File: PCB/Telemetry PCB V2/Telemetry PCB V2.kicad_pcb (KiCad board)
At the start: 4 copper layers, 70 x 70 mm, 51 parts, among them IC1 E22-900M22S, J1 USB_C_Receptacle_USB2.0_16P, J2 DBG/PGRM Hdr., J3 DATA IN, J4 GPS, J5 Battery, SW1 SW_MEC_5E, SW2 SW_MEC_5E, U1 STM32F411CEUx, U2 MCP1700x-250xxTT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

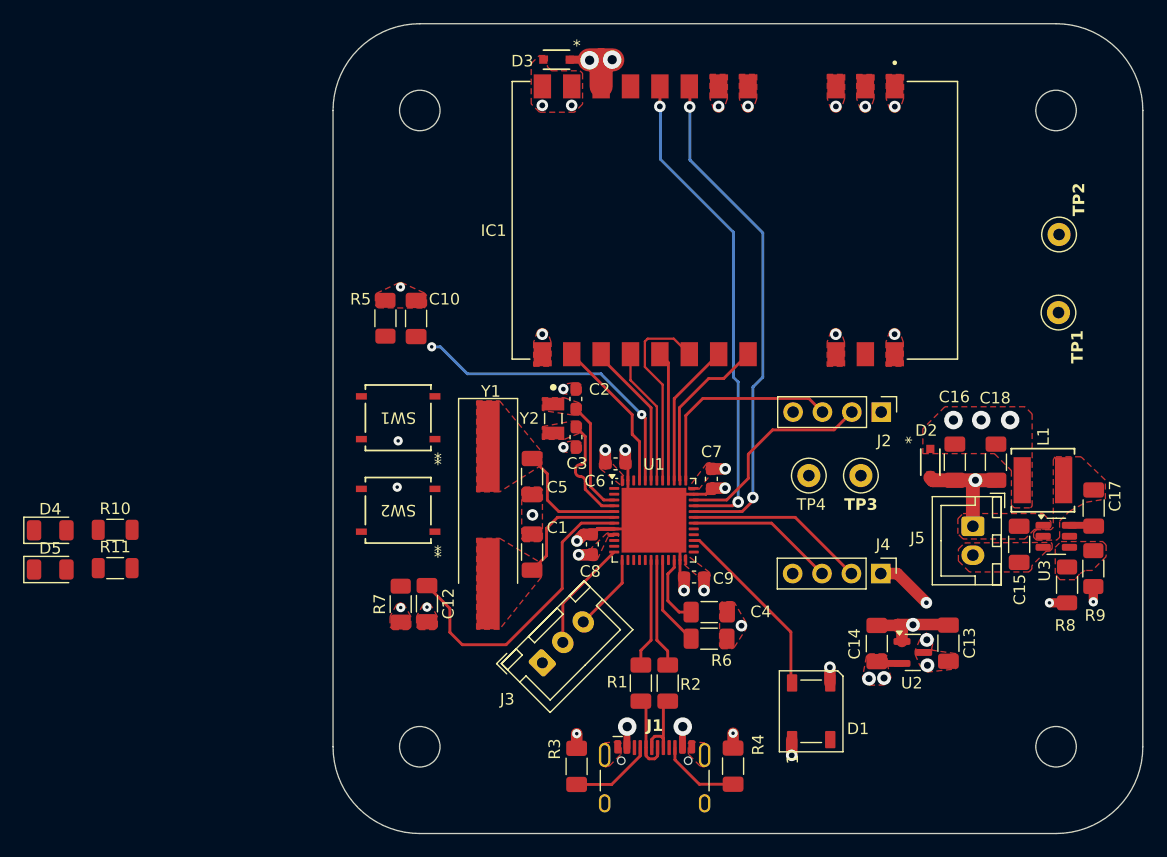
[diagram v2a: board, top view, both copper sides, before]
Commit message: Finished updating board to reflect issues and new components
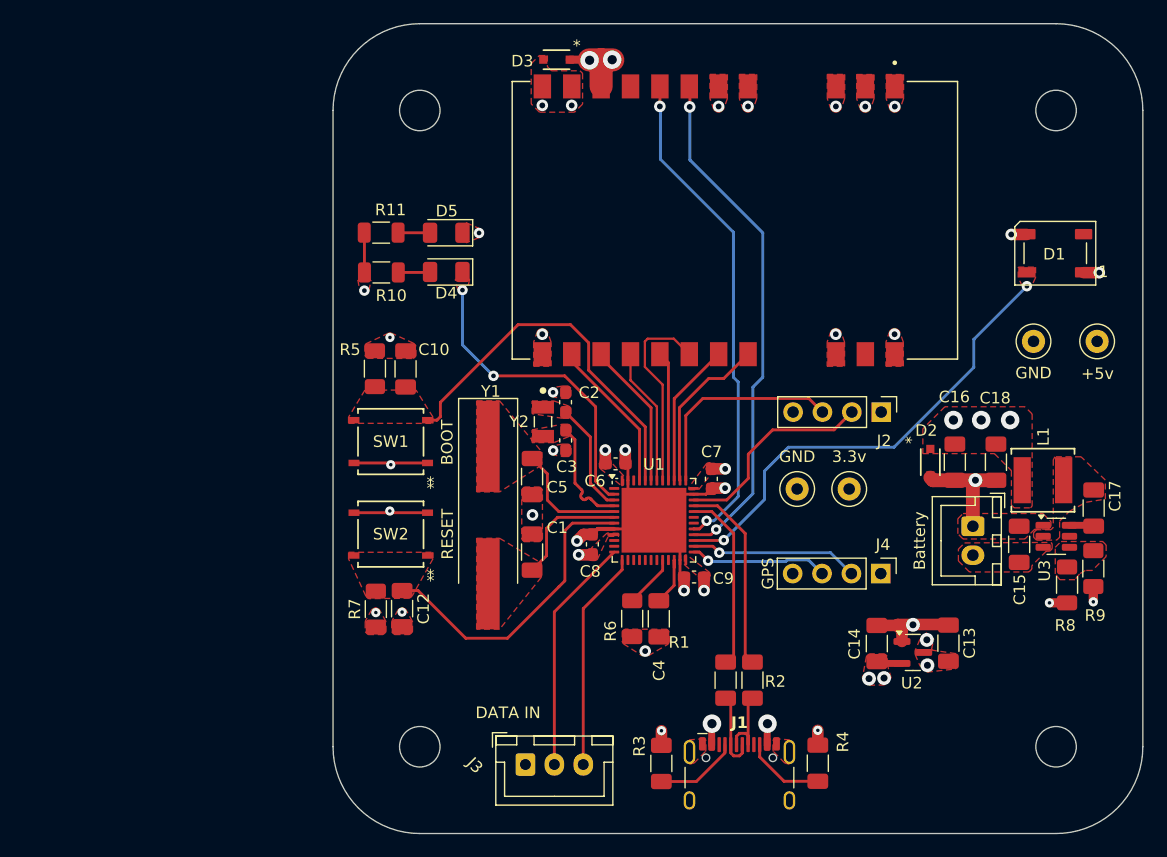
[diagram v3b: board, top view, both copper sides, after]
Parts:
- SW1: value SW_MEC_5E -> BOOT
- SW2: value SW_MEC_5E -> RESET
- TP1, TP4: value TestPoint -> GND
- TP2: value TestPoint -> +5v
- TP3: value TestPoint -> 3.3v
- moved D5 44.9 mm to (132.7, 66.5), turned to 180 degrees
- moved D1 44.9 mm to (185.3, 68.3), turned to 180 degrees
- moved D4 40.9 mm to (132.7, 69.9), turned to 180 degrees
- moved R11 37.0 mm to (127.0, 66.5)
- moved R10 32.0 mm to (127.0, 69.9)
- moved TP2 9.81 mm to (188.9, 75.9)
- moved J3 8.91 mm to (139.5, 112.5), turned to 0 degrees
- moved R1 7.33 mm to (156.8, 105.2)
- moved R4 7.33 mm to (164.8, 112.4)
- moved J1 7.33 mm to (158.0, 114.5)
- moved R2 7.33 mm to (159.1, 105.2)
- moved R3 7.33 mm to (151.2, 112.4)
- moved R6 6.87 mm to (148.7, 99.9), turned to 90 degrees
- moved C10 4.45 mm to (129.1, 78.3)
- moved R5 4.45 mm to (126.5, 78.3)
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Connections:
- U1 pad 2: unconnected-(U1-PC13-Pad2) -> PC13
- U1 pad 25: unconnected-(U1-PB12-Pad25) -> TX
- U1 pad 26: unconnected-(U1-PB13-Pad26) -> RX
- U1 pad 30: TX -> unconnected-(U1-PA9-Pad30)
- U1 pad 31: RX -> unconnected-(U1-PA10-Pad31)
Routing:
- net PC13: track 0.00 -> 27.0 mm, vias 0 -> 2
- net DIN: track 16.1 -> 40.8 mm, vias 0 -> 2
- net (no net): track 18.9 -> 0.00 mm
- net Net-(U1-PA12): track 0.00 -> 16.8 mm
- net Net-(U1-PA11): track 0.00 -> 16.0 mm
- net RX2: track 6.75 -> 19.1 mm
- net TX2: track 9.65 -> 20.5 mm
- net +3.3V: track 7.50 -> 17.3 mm, vias 8 -> 9
- net GND: track 52.3 -> 58.7 mm, vias 27 -> 28
- net BOOT0: track 26.4 -> 32.7 mm, vias 2 -> 0
- net +5V: track 17.4 -> 12.4 mm, vias 12 -> 11
- net PB2: track 7.82 -> 4.61 mm
- net Net-(D5-A): track 0.00 -> 2.77 mm
- net Net-(D4-A): track 0.00 -> 2.76 mm
- net RX: track 15.6 -> 14.6 mm, vias 0 -> 1
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- added copper zone on F.Cu, net BOOT0
- added copper zone on F.Cu, net DIN
- added copper zone on F.Cu, net NRST
- added copper zone on F.Cu, net PC13

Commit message: Started adding labels
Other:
- board text added: "3.3v"
- board text added: "5v"
- board text added: "CLK"
- board text added: "DIO"
- board text added: "GND"
- board text added: "RX"
- board text added: "TX"
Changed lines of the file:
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@@
 		)
 		(property "Value" "3.3v"
-			(at 0 -2.8 0)
+			(at 0.14 2.73 0)
 			(layer "F.SilkS")
 			(effects
@@
 		)
 		(property "Value" "GND"
-			(at 0 -2.8 0)
+			(at -0.07 2.78 0)
 			(layer "F.SilkS")
 			(effects
@@
 		(layer "Edge.Cuts")
 	)
+	(gr_text "TX"
+		(at 164.34 98.9 0)
+		(layer "F.SilkS")
+		(effects
+			(font
+				(size 0.8 0.8)
+				(thickness 0.16)
+				(bold yes)
+			)
+			(justify left bottom)
+		)
+	)
+	(gr_text "CLK"
+		(at 163.92 80.04 0)
+		(layer "F.SilkS")
+		(effects
+			(font
+				(size 0.8 0.8)
+				(thickness 0.16)
+				(bold yes)
+			)
+			(justify left bottom)
+		)
+	)
+	(gr_text "RX"
+		(at 166.81 98.85 0)
+		(layer "F.SilkS")
+		(effects
+			(font
+				(size 0.8 0.8)
+				(thickness 0.16)
+				(bold yes)
+			)
+			(justify left bottom)
+		)
+	)
+	(gr_text "GND\n"
+		(at 161.24 98.9 0)
+		(layer "F.SilkS")
+		(effects
+			(font
+				(size 0.8 0.8)
+				(thickness 0.16)
+				(bold yes)
+			)
+			(justify left bottom)
+		)
+	)
+	(gr_text "5v"
+		(at 169.48 98.84 0)
+		(layer "F.SilkS")
+		(effects
+			(font
+				(size 0.8 0.8)
+				(thickness 0.16)
+				(bold yes)
+			)
+			(justify left bottom)
+		)
+	)
+	(gr_text "GND\n"
+		(at 161.24 80.03 0)
+		(layer "F.SilkS")
+		(effects
+			(font
+				(size 0.8 0.8)
+				(thickness 0.16)
+				(bold yes)
+			)
+			(justify left bottom)
+		)
+	)
+	(gr_text "DIO\n"
+		(at 166.58 80.09 0)
+		(layer "F.SilkS")
+		(effects
+			(font
+				(size 0.8 0.8)
+				(thickness 0.16)
+				(bold yes)
+			)
+			(justify left bottom)
+		)
+	)
+	(gr_text "3.3v"
+		(at 169.13 80.13 0)
+		(layer "F.SilkS")
+		(effects
+			(font
+				(size 0.8 0.8)
+				(thickness 0.16)
+				(bold yes)
+			)
+			(justify left bottom)
+		)
+	)
 	(dimension

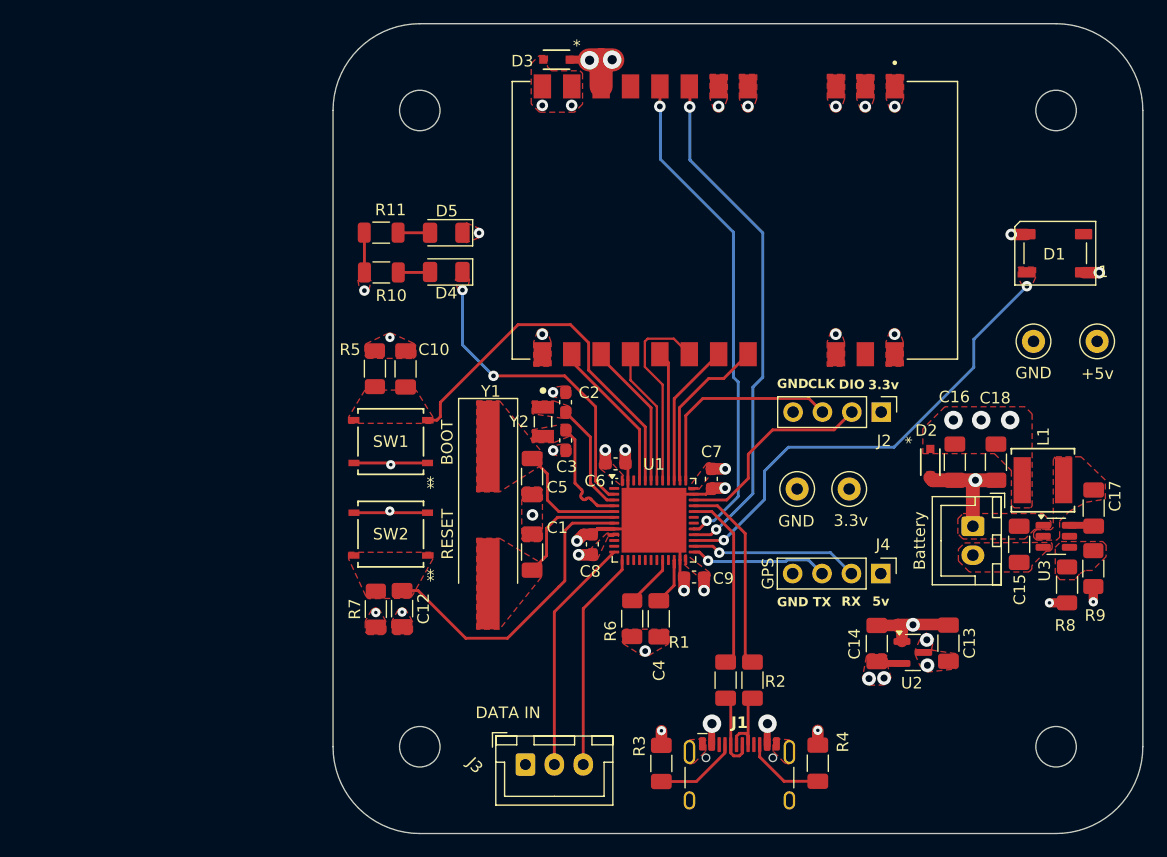
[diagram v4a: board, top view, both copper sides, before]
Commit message: Finished adding labels, fixed DRC violations
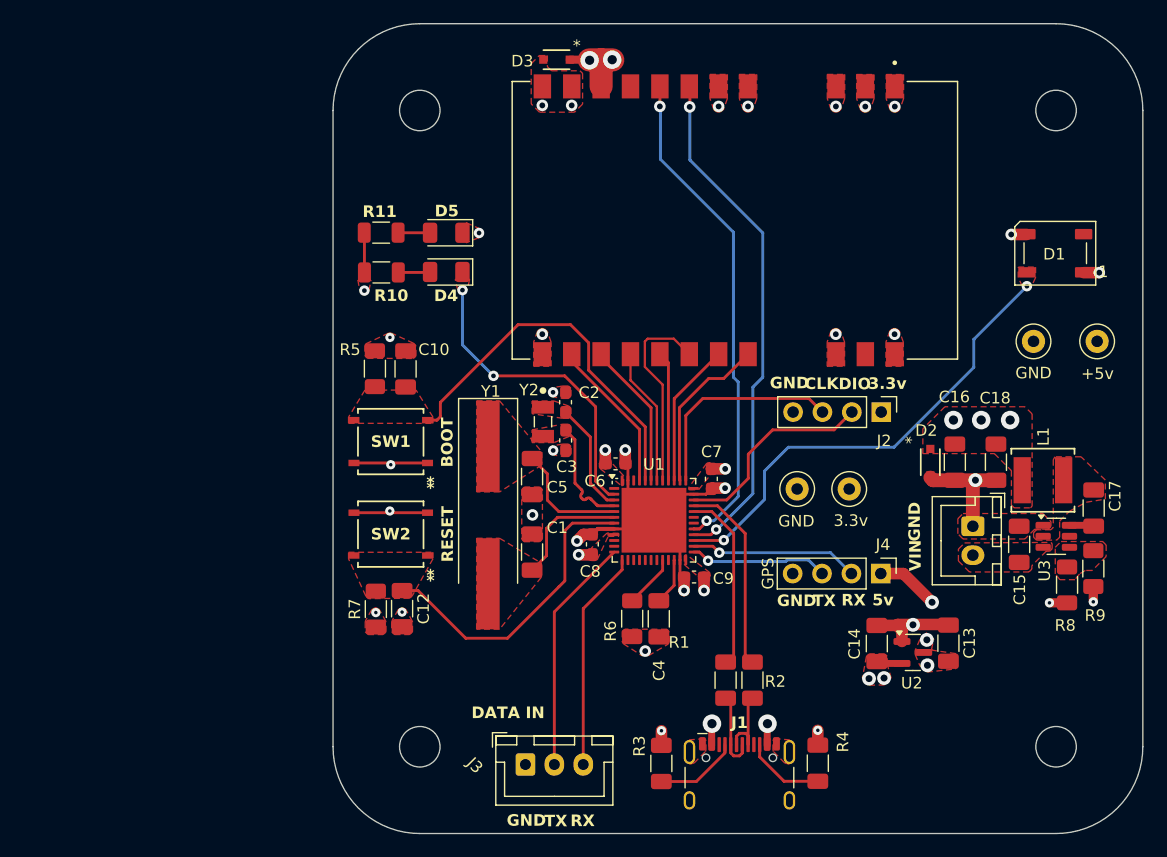
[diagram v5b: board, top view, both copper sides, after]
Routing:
- net +5V: track 12.4 -> 17.9 mm, vias 11 -> 12
- net Net-(U1-VCAP1): track 5.23 -> 4.57 mm
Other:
- board text added: "VIN"
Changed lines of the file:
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@@
 				(font
 					(size 1 1)
-					(thickness 0.15)
+					(thickness 0.18)
+					(bold yes)
 				)
 			)
@@
 				(font
 					(size 1 1)
-					(thickness 0.15)
+					(thickness 0.18)
+					(bold yes)
 				)
 			)
@@
 				(font
 					(size 1 1)
-					(thickness 0.15)
+					(thickness 0.18)
+					(bold yes)
 				)
 			)
@@
 				(font
 					(size 1 1)
-					(thickness 0.15)
+					(thickness 0.18)
+					(bold yes)
 				)
 			)
@@
 				(font
 					(size 1 1)
-					(thickness 0.15)
+					(thickness 0.18)
+					(bold yes)
 				)
 			)
@@
 				(font
 					(size 1 1)
-					(thickness 0.15)
+					(thickness 0.18)
+					(bold yes)
 				)
 			)
@@
 				(font
 					(size 1 1)
-					(thickness 0.15)
+					(thickness 0.18)
+					(bold yes)
 				)
 			)
@@
 				(font
 					(size 1 1)
-					(thickness 0.15)
+					(thickness 0.18)
+					(bold yes)
 				)
 			)
@@
 				(font
 					(size 1 1)
-					(thickness 0.15)
+					(thickness 0.18)
+					(bold yes)
 				)
 			)
@@
 		(at 141.02 82.850001 -90)
 		(property "Reference" "Y2"
-			(at -0.010001 2.07 0)
+			(at -2.750001 1.21 0)
 			(layer "F.SilkS")
 			(effects
@@
 				(font
 					(size 1 1)
-					(thickness 0.15)
+					(thickness 0.18)
+					(bold yes)
 				)
 			)
@@
 				(font
 					(size 1 1)
-					(thickness 0.15)
+					(thickness 0.18)
+					(bold yes)
 				)
 			)
@@
 		(tags "LED")
 		(property "Reference" "D4"
-			(at 0 -1.83 0)
+			(at 0.0175 -2.05 0)
 			(layer "F.SilkS")
 			(effects
 				(font
 					(size 1 1)
-					(thickness 0.15)
+					(thickness 0.18)
+					(bold yes)
 				)
 			)
@@
 		(tags "resistor")
 		(property "Reference" "R11"
-			(at 0.81 -1.97 0)
+			(at -0.13 -1.82 0)
 			(layer "F.SilkS")
 			(effects
 				(font
 					(size 1 1)
-					(thickness 0.15)
+					(thickness 0.18)
+					(bold yes)
 				)
 			)
@@
 		)
 		(property "Value" "Battery"
-			(at 1.25 4.6 270)
-			(layer "F.SilkS")
+			(at 1.25 1.948899 270)
+			(layer "F.Fab")
 			(effects
 				(font
@@
 		(effects
 			(font
-				(size 0.8 0.8)
-				(thickness 0.16)
+				(size 1 1)
+				(thickness 0.18)
 				(bold yes)
 			)
@@
 	)
 	(gr_text "CLK"
-		(at 163.92 80.04 0)
+		(at 163.63 80.14 0)
+		(layer "F.SilkS")
+		(effects
+			(font
+				(size 1 1)
+				(thickness 0.18)
+				(bold yes)
+			)
+			(justify left bottom)
+		)
+	)
+	(gr_text "GND\n"
+		(at 137.88 117.89 0)
 		(layer "F.SilkS")
 		(effects
 			(font
-				(size 0.8 0.8)
-				(thickness 0.16)
+				(size 1 1)
+				(thickness 0.18)
+				(bold yes)
+			)
+			(justify left bottom)
+		)
+	)
+	(gr_text "TX\n"
+		(at 141.13 117.94 0)
+		(layer "F.SilkS")
+		(effects
+			(font
+				(size 1 1)
+				(thickness 0.18)
 				(bold yes)
 			)
@@
 		(effects
 			(font
-				(size 0.8 0.8)
-				(thickness 0.16)
+				(size 1 1)
+				(thickness 0.18)
 				(bold yes)
 			)
@@
 		(effects
 			(font
-				(size 0.8 0.8)
-				(thickness 0.16)
+				(size 1 1)
+				(thickness 0.18)
 				(bold yes)
 			)
@@
 		(effects
 			(font
-				(size 0.8 0.8)
-				(thickness 0.16)
+				(size 1 1)
+				(thickness 0.18)
 				(bold yes)
 			)
@@
 	)
 	(gr_text "GND\n"
-		(at 161.24 80.03 0)
+		(at 160.62 80.08 0)
+		(layer "F.SilkS")
+		(effects
+			(font
+				(size 1 1)
+				(thickness 0.18)
+				(bold yes)
+			)
+			(justify left bottom)
+		)
+	)
+	(gr_text "VIN\n"
+		(at 173.79 95.77 90)
+		(layer "F.SilkS")
+		(effects
+			(font
+				(size 1 1)
+				(thickness 0.18)
+				(bold yes)
+			)
+			(justify left bottom)
+		)
+	)
+	(gr_text "RX\n"
+		(at 143.38 117.92 0)
 		(layer "F.SilkS")
 		(effects
 			(font
-				(size 0.8 0.8)
-				(thickness 0.16)
+				(size 1 1)
+				(thickness 0.18)
 				(bold yes)
 			)
@@
 	)
 	(gr_text "DIO\n"
-		(at 166.58 80.09 0)
+		(at 166.56 80.16 0)
 		(layer "F.SilkS")
 		(effects
 			(font
-				(size 0.8 0.8)
-				(thickness 0.16)
+				(size 1 1)
+				(thickness 0.18)
 				(bold yes)
 			)
@@
 		(effects
 			(font
-				(size 0.8 0.8)
-				(thickness 0.16)
+				(size 1 1)
+				(thickness 0.18)
+				(bold yes)
+			)
+			(justify left bottom)
+		)
+	)
+	(gr_text "GND\n"
+		(at 173.72 93.19 90)
+		(layer "F.SilkS")
+		(effects
+			(font
+				(size 1 1)
+				(thickness 0.18)
 				(bold yes)
 			)
@@
 	)
 	(segment
-		(start 152.3625 95.45)
-		(end 152.3625 94.7975)
-		(width 0.25)
-		(layer "F.Cu")
-		(net 5)
-	)
-	(segment
 		(start 152.3625 94.7975)
 		(end 152.351499 94.808501)
@@
 	)
 	(segment
+		(start 174.65 98.45)
+		(end 172.17 95.97)
+		(width 1)
+		(layer "F.Cu")
+		(net 10)
+	)
+	(segment
 		(start 160.4 110.82)
 		(end 160.4 108.96)
@@
 	)
 	(segment
+		(start 172.17 95.97)
+		(end 170.22 95.97)
+		(width 1)
+		(layer "F.Cu")
+		(net 10)
+	)
+	(segment
 		(start 187.755 69.96)
 		(end 189.104999 69.96)
@@
 	)
 	(via
+		(at 174.65 98.45)
+		(size 1.2)
+		(drill 0.6)
+		(layers "F.Cu" "B.Cu")
+		(free yes)
+		(net 10)
+	)
+	(via
 		(at 147 51.55)
 		(size 1.6)
@@
 	)
 	(zone
-		(net 23)
-		(net_name "TXEN")
-		(layer "F.Cu")
-		(name "$teardrop_padvia$")
-		(hatch none 0.1)
-		(priority 30001)
-		(attr
-			(teardrop
-				(type padvia)
-			)
-		)
-		(connect_pads yes
-			(clearance 0)
-		)
-		(min_thickness 0.0254)
-		(filled_areas_thickness no)
-		(fill yes
-			(thermal_gap 0.5)
-			(thermal_bridge_width 0.5)
-			(island_removal_mode 1)
-			(island_area_min 10)
-		)
-		(polygon
-			(pts
-				(xy 151.255 54.599607) (xy 151.005 54.599607) (xy 150.704265 55.312215) (xy 151.12 55.591) (xy 151.610393 55.492455)
-			)
-		)
-	)
-	(zone
 		(net 2)
 		(net_name "Net-(U1-PH1)")
@@
 	)
 	(zone
-		(net 20)
-		(net_name "RXEN")
-		(layer "F.Cu")
-		(name "$teardrop_padvia$")
-		(hatch none 0.1)
-		(priority 30000)
-		(attr
-			(teardrop
-				(type padvia)
-			)
-		)
-		(connect_pads yes
-			(clearance 0)
-		)
-		(min_thickness 0.0254)
-		(filled_areas_thickness no)
-		(fill yes
-			(thermal_gap 0.5)
-			(thermal_bridge_width 0.5)
-			(island_removal_mode 1)
-			(island_area_min 10)
-		)
-		(polygon
-			(pts
-				(xy 153.845 54.639607) (xy 153.595 54.639607) (xy 153.284265 55.352215) (xy 153.7 55.631) (xy 154.190393 55.532455)
-			)
-		)
-	)
-	(zone
 		(net 6)
 		(net_name "Net-(U1-PH0)")
@@
 	)
 	(zone
+		(net 20)
+		(net_name "RXEN")
+		(layer "F.Cu")
+		(name "$teardrop_padvia$")
+		(hatch none 0.1)
+		(priority 30000)
+		(attr
+			(teardrop
+				(type padvia)
+			)
+		)
+		(connect_pads yes
+			(clearance 0)
+		)
+		(min_thickness 0.0254)
+		(filled_areas_thickness no)
+		(fill yes
+			(thermal_gap 0.5)
+			(thermal_bridge_width 0.5)
+			(island_removal_mode 1)
+			(island_area_min 10)
+		)
+		(polygon
+			(pts
+				(xy 153.845 54.639607) (xy 153.595 54.639607) (xy 153.284265 55.352215) (xy 153.7 55.631) (xy 154.190393 55.532455)
+			)
+		)
+	)
+	(zone
 		(net 1)
 		(net_name "GND")
@@
 			)
 		)
+	)
+	(zone
+		(net 23)
+		(net_name "TXEN")
+		(layer "F.Cu")
+		(name "$teardrop_padvia$")
+		(hatch none 0.1)
+		(priority 30001)
+		(attr
+			(teardrop
+				(type padvia)
+			)
+		)
+		(connect_pads yes
+			(clearance 0)
+		)
+		(min_thickness 0.0254)
+		(filled_areas_thickness no)
+		(fill yes
+			(thermal_gap 0.5)
+			(thermal_bridge_width 0.5)
+			(island_removal_mode 1)
+			(island_area_min 10)
+		)
+		(polygon
+			(pts
+				(xy 151.255 54.599607) (xy 151.005 54.599607) (xy 150.704265 55.312215) (xy 151.12 55.591) (xy 151.610393 55.492455)
+			)
+		)

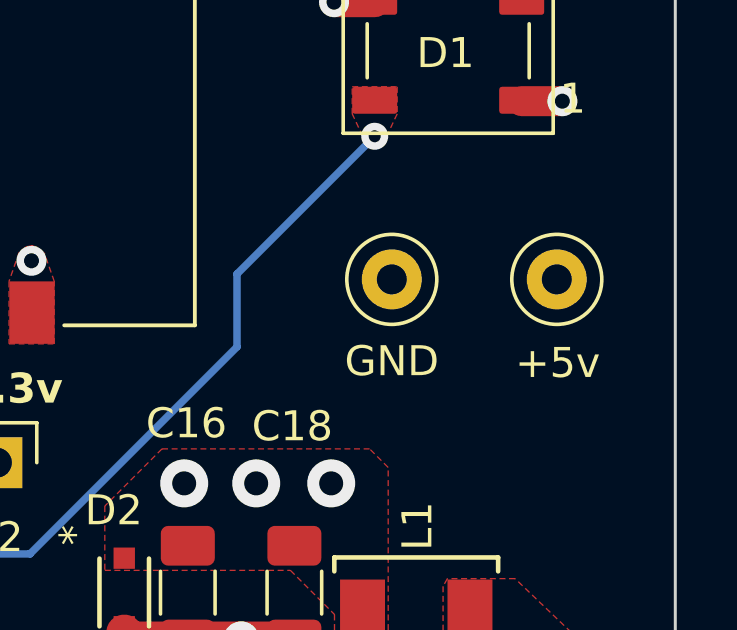
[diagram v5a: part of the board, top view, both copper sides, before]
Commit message: Moved some components
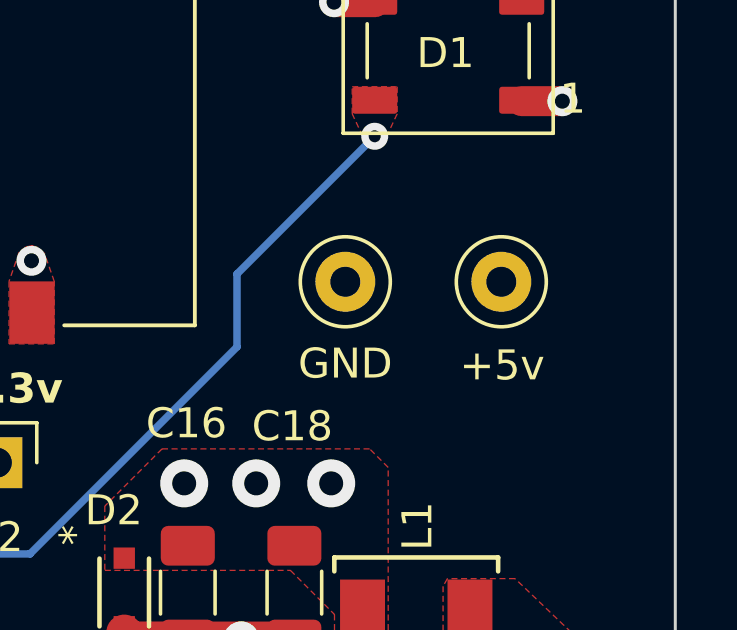
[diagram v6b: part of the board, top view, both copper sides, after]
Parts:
- moved TP2 1.85 mm to (187.1, 76.0)
- moved TP1 1.55 mm to (181.9, 76.0)
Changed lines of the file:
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@@
 	(footprint "TestPoint:TestPoint_Loop_D1.80mm_Drill1.0mm_Beaded"
 		(layer "F.Cu")
-		(at 183.42 75.9 90)
+		(at 181.87 75.98 90)
 		(descr "wire loop with bead as test point, loop diameter 1.8mm, hole diameter 1.0mm")
 		(tags "test point wire loop bead")
@@
 	(footprint "TestPoint:TestPoint_Loop_D1.80mm_Drill1.0mm_Beaded"
 		(layer "F.Cu")
-		(at 188.92 75.9 90)
+		(at 187.07 75.98 90)
 		(descr "wire loop with bead as test point, loop diameter 1.8mm, hole diameter 1.0mm")
 		(tags "test point wire loop bead")
